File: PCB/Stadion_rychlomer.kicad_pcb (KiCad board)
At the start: 4 copper layers, 44 x 44 mm, 56 parts, among them J2 OLED I2C, J3 ICSP, J4 Conn_01x03_Pin, J5 SPÍD & PWR, J6 AUX DDAA, J7 ENG RPM, Q1 140817143200, Q2 PC817, U1 Mikroprofesor, U3 LM1117MP-5.0, Y1 16MHz

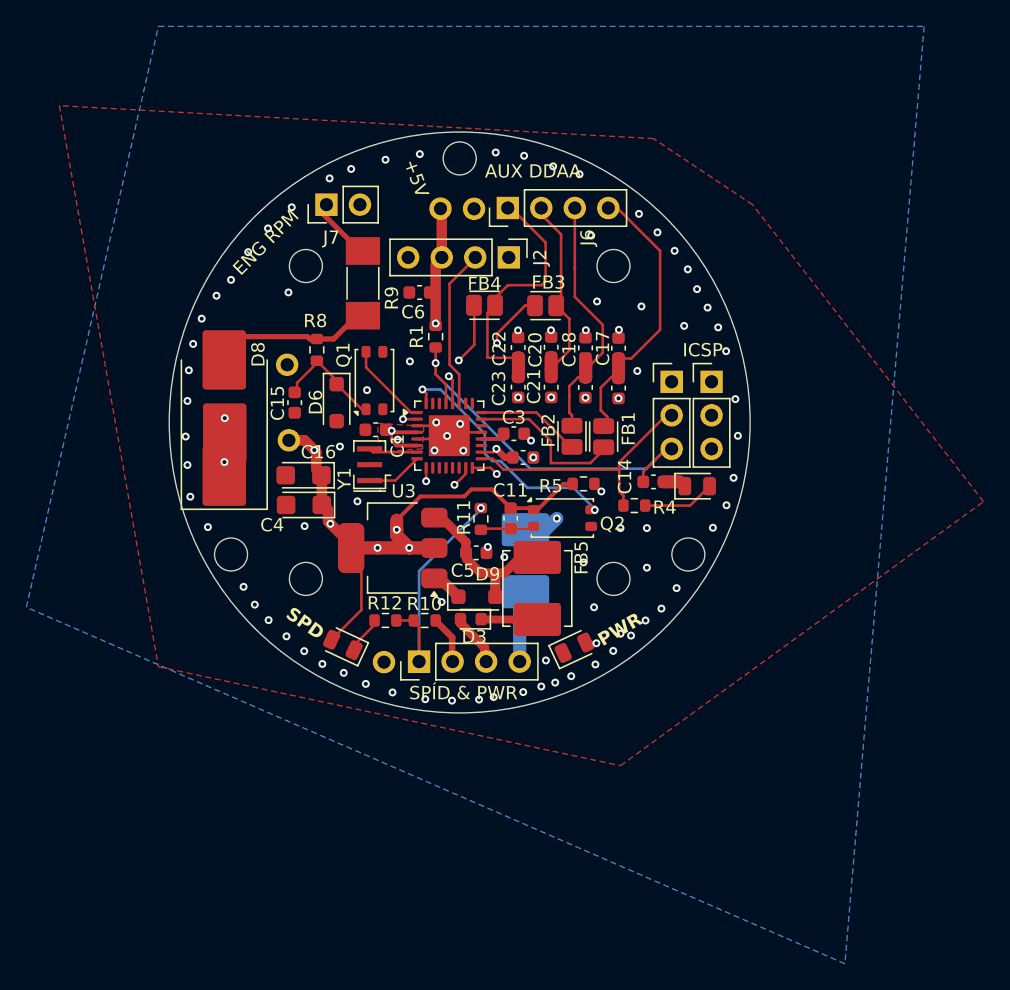
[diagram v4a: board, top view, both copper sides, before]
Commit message: SCL SDA Fixed, minor edits
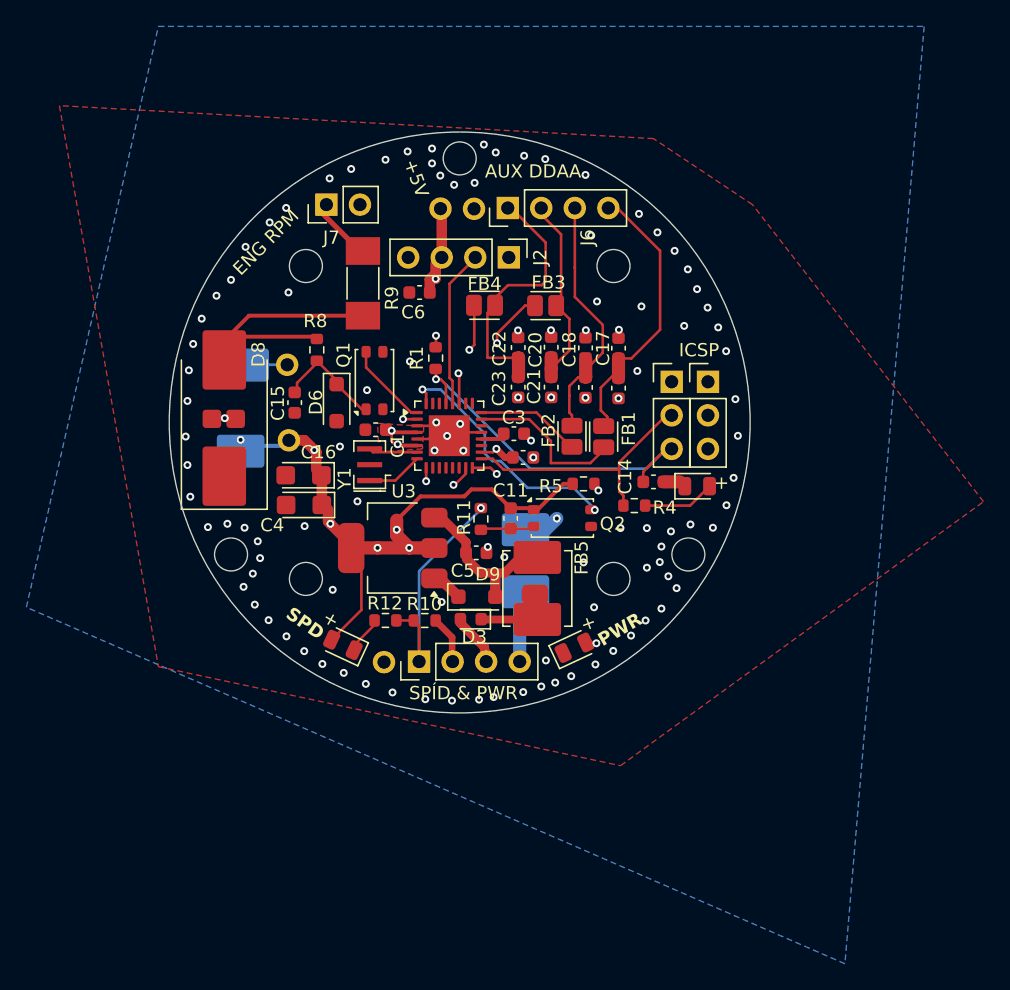
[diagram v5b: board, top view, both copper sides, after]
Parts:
- removed the ? at (100.0, 144.8)
- added ?: , , F.Cu at (123.5, 157.0)
- added ?: , , F.Cu at (101.2, 146.2)
- added ?: , , F.Cu at (100.8, 143.7)
- added ?: , , F.Cu at (99.0, 143.7)
- added ?: , , F.Cu at (101.6, 139.7)
- D9: value SMCJ85CA -> PTVS8V5S1UTR-QX
- FB5, FB6: value FerriteBead_Small -> FerriteBead_4A_180Ω
- moved R1 1.62 mm to (116.0, 139.1)
- moved J3 0.28 mm to (136.6, 140.9)
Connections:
- C5 pad 1: Net-(D9-A2) -> Net-(D9-K)
- D9 pad 1: GND -> Net-(D9-K)
- D9 pad 2: Net-(D9-A2) -> GND
- FB5 pad 2: Net-(D9-A2) -> Net-(D9-K)
- U1 pad 27: /I2C_SCL -> /I2C_SDA
- U1 pad 28: /I2C_SDA -> /I2C_SCL
- U3 pad 3: Net-(D9-A2) -> Net-(D9-K)
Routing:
- net +5V: track 118.4 -> 97.9 mm, vias 13 -> 15
- net GND: track 16.7 -> 32.1 mm, vias 92 -> 107
- net Net-(D9-A2): track 12.0 -> 0.00 mm
- net Net-(D8-A2): track 11.1 -> 20.1 mm
- net /I2C_SDA: track 16.7 -> 12.7 mm
- net /RESET_: track 29.8 -> 27.4 mm
- net /D4: track 14.9 -> 14.2 mm
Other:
- board text added: "+"
- board text added: "MOPeD JeSUS STADi-SPÍDo V2"
- board text removed: "MOPeD JeSUS STADi-SPÍDo V1"

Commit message: fix TVS na VIN
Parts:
- moved D9 0.06 mm to (119.1, 157.2), turned to 180 degrees
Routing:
- net Net-(D9-K): track 0.00 -> 12.0 mm
- net GND: track 32.1 -> 20.1 mm
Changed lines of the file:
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@@
 	(footprint "Diode_SMD:D_SOD-123F"
 		(layer "F.Cu")
-		(at 119.125 157.2)
+		(at 119.1 157.15 180)
 		(descr "D_SOD-123F")
 		(tags "D_SOD-123F")
 		(property "Reference" "D9"
-			(at 0.825 -1.7 0)
+			(at 0.825 -1.7 180)
 			(layer "F.SilkS")
 			(effects
@@
 		)
 		(property "Value" "PTVS8V5S1UTR-QX"
-			(at 0 2.1 0)
+			(at 0 2.1 180)
 			(layer "F.Fab")
 			(hide yes)
@@
 		)
 		(property "Datasheet" "https://assets.nexperia.com/documents/data-sheet/PTVSXS1UTR-Q_SER.pdf"
-			(at 0 0 0)
+			(at 0 0 180)
 			(unlocked yes)
 			(layer "F.Fab")
@@
 		)
 		(property "Description" "Ochranné diody proti elektrostatickým výbojům/diody pro potlačení napětí z přechodových jevů PTVS8V5S1UTR-Q/SOD123W/CFP3"
-			(at 0 0 0)
+			(at 0 0 180)
 			(unlocked yes)
 			(layer "F.Fab")
@@
 		)
 		(property "PN" " PTVS8V5S1UTR-QX "
-			(at 0 0 0)
+			(at 0 0 180)
 			(unlocked yes)
 			(layer "F.Fab")
@@
 		)
 		(property "Supplier PN" " 771-PTVS8V5S1UTR-QX "
-			(at 0 0 0)
+			(at 0 0 180)
 			(unlocked yes)
 			(layer "F.Fab")
@@
 		)
 		(property "Supplier" "Mouser Electronics"
-			(at 0 0 0)
+			(at 0 0 180)
 			(unlocked yes)
 			(layer "F.Fab")
@@
 		)
 		(property "JLCPCB Part" ""
-			(at 0 0 0)
+			(at 0 0 180)
 			(unlocked yes)
 			(layer "F.Fab")
@@
 		(duplicate_pad_numbers_are_jumpers no)
 		(fp_line
-			(start -2.21 -1)
-			(end -2.21 1)
+			(start -2.21 1)
+			(end 1.65 1)
 			(stroke
 				(width 0.12)
@@
 		)
 		(fp_line
-			(start -2.21 1)
-			(end 1.65 1)
+			(start -2.21 -1)
+			(end -2.21 1)
 			(stroke
 				(width 0.12)
@@
 		)
 		(fp_line
-			(start -2.2 -1.15)
+			(start 2.2 1.15)
 			(end -2.2 1.15)
 			(stroke
@@
 		)
 		(fp_line
-			(start -2.2 -1.15)
-			(end 2.2 -1.15)
+			(start 2.2 -1.15)
+			(end 2.2 1.15)
 			(stroke
 				(width 0.05)
@@
 		)
 		(fp_line
-			(start 2.2 -1.15)
-			(end 2.2 1.15)
+			(start -2.2 -1.15)
+			(end 2.2 -1.15)
 			(stroke
 				(width 0.05)
@@
 		)
 		(fp_line
-			(start 2.2 1.15)
+			(start -2.2 -1.15)
 			(end -2.2 1.15)
 			(stroke
@@
 		)
 		(fp_line
-			(start -1.4 -0.9)
-			(end 1.4 -0.9)
+			(start 1.4 0.9)
+			(end -1.4 0.9)
 			(stroke
 				(width 0.1)
@@
 		)
 		(fp_line
-			(start -1.4 0.9)
-			(end -1.4 -0.9)
+			(start 1.4 -0.9)
+			(end 1.4 0.9)
 			(stroke
 				(width 0.1)
@@
 		)
 		(fp_line
-			(start -0.75 0)
+			(start 0.25 0.4)
 			(end -0.35 0)
 			(stroke
@@
 		)
 		(fp_line
-			(start -0.35 0)
-			(end -0.35 -0.55)
+			(start 0.25 0)
+			(end 0.75 0)
 			(stroke
 				(width 0.1)
@@
 		)
 		(fp_line
-			(start -0.35 0)
-			(end -0.35 0.55)
+			(start 0.25 -0.4)
+			(end 0.25 0.4)
 			(stroke
 				(width 0.1)
@@
 		)
 		(fp_line
-			(start 0.25 -0.4)
-			(end 0.25 0.4)
+			(start -0.35 0)
+			(end -0.35 0.55)
 			(stroke
 				(width 0.1)
@@
 		)
 		(fp_line
-			(start 0.25 0)
-			(end 0.75 0)
+			(start -0.35 0)
+			(end -0.35 -0.55)
 			(stroke
 				(width 0.1)
@@
 		)
 		(fp_line
-			(start 0.25 0.4)
+			(start -0.75 0)
 			(end -0.35 0)
 			(stroke
@@
 		)
 		(fp_line
-			(start 1.4 -0.9)
-			(end 1.4 0.9)
+			(start -1.4 0.9)
+			(end -1.4 -0.9)
 			(stroke
 				(width 0.1)
@@
 		)
 		(fp_line
-			(start 1.4 0.9)
-			(end -1.4 0.9)
+			(start -1.4 -0.9)
+			(end 1.4 -0.9)
 			(stroke
 				(width 0.1)
@@
 		)
 		(fp_text user "${REFERENCE}"
-			(at 0.825 -1.7 0)
+			(at 0.825 -1.7 180)
 			(layer "F.Fab")
 			(effects
@@
 		)
 		(pad "1" smd roundrect
-			(at -1.4 0)
+			(at -1.4 0 180)
 			(size 1.1 1.1)
 			(layers "F.Cu" "F.Mask" "F.Paste")
@@
 		)
 		(pad "2" smd roundrect
-			(at 1.4 0)
+			(at 1.4 0 180)
 			(size 1.1 1.1)
 			(layers "F.Cu" "F.Mask" "F.Paste")
@@
 	)
 	(segment
-		(start 116.15 151.2)
-		(end 116.425 151.2)
-		(width 0.5)
-		(layer "F.Cu")
-		(net "GND")
-	)
-	(segment
 		(start 117 144.97)
 		(end 116.28 144.25)
@@
 	)
 	(segment
-		(start 120.525 157.2)
-		(end 120.525 155.475)
-		(width 0.8)
-		(layer "F.Cu")
-		(net "GND")
-	)
-	(segment
 		(start 113.46 131.96)
 		(end 113.92 131.5)
@@
 	)
 	(segment
-		(start 120.6 155.4)
-		(end 121.225 155.4)
-		(width 0.7)
-		(layer "F.Cu")
-		(net "GND")
-	)
-	(segment
 		(start 116.953114 145.076886)
 		(end 116.78 145.25)
@@
 	)
 	(segment
-		(start 121.225 155.4)
-		(end 122.325 154.3)
-		(width 0.7)
-		(layer "F.Cu")
-		(net "GND")
-	)
-	(segment
 		(start 116.840735 145.189265)
 		(end 115.531765 145.189265)
@@
 	)
 	(segment
-		(start 122.325 154.3)
-		(end 123.4 154.3)
-		(width 0.7)
-		(layer "F.Cu")
-		(net "GND")
-	)
-	(segment
 		(start 117 145.016943)
 		(end 117 144.97)
@@
 	)
 	(segment
-		(start 120.525 155.475)
-		(end 120.6 155.4)
-		(width 0.2)
-		(layer "F.Cu")
-		(net "GND")
-	)
-	(segment
 		(start 117.725 157.2)
 		(end 116.3375 155.8125)
@@
 	)
 	(segment
-		(start 118.3 153.075)
-		(end 118.3 153.875)
-		(width 0.7)
-		(layer "F.Cu")
-		(net "GND")
-	)
-	(segment
 		(start 114.225 131.195)
 		(end 113.92 131.5)
@@
 	)
 	(segment
-		(start 119.4 155.4)
-		(end 120.6 155.4)
-		(width 0.7)
-		(layer "F.Cu")
-		(net "GND")
-	)
-	(segment
-		(start 118.35 153.925)
-		(end 118.35 154.35)
-		(width 0.7)
-		(layer "F.Cu")
-		(net "GND")
-	)
-	(segment
 		(start 112.131372 143)
 		(end 112 143)
@@
 	)
 	(segment
-		(start 118.3 153.875)
-		(end 118.35 153.925)
-		(width 0.7)
-		(layer "F.Cu")
-		(net "GND")
-	)
-	(segment
 		(start 117 145.03)
 		(end 116.953114 145.076886)
@@
 		(net "GND")
 	)
-	(segment
-		(start 118.35 154.35)
-		(end 119.4 155.4)
-		(width 0.7)
-		(layer "F.Cu")
-		(net "GND")
-	)
-	(segment
-		(start 116.425 151.2)
-		(end 118.3 153.075)
-		(width 0.7)
-		(layer "F.Cu")
-		(net "GND")
-	)
 	(via
 		(at 131.4 128.2)
@@
 	)
 	(segment
+		(start 116.15 151.2)
+		(end 116.425 151.2)
+		(width 0.5)
+		(layer "F.Cu")
+		(net "Net-(D9-K)")
+	)
+	(segment
+		(start 120.525 157.2)
+		(end 120.525 155.475)
+		(width 0.8)
+		(layer "F.Cu")
+		(net "Net-(D9-K)")
+	)
+	(segment
+		(start 120.6 155.4)
+		(end 121.225 155.4)
+		(width 0.7)
+		(layer "F.Cu")
+		(net "Net-(D9-K)")
+	)
+	(segment
+		(start 121.225 155.4)
+		(end 122.325 154.3)
+		(width 0.7)
+		(layer "F.Cu")
+		(net "Net-(D9-K)")
+	)
+	(segment
+		(start 122.325 154.3)
+		(end 123.4 154.3)
+		(width 0.7)
+		(layer "F.Cu")
+		(net "Net-(D9-K)")
+	)
+	(segment
+		(start 120.525 155.475)
+		(end 120.6 155.4)
+		(width 0.2)
+		(layer "F.Cu")
+		(net "Net-(D9-K)")
+	)
+	(segment
+		(start 118.3 153.075)
+		(end 118.3 153.875)
+		(width 0.7)
+		(layer "F.Cu")
+		(net "Net-(D9-K)")
+	)
+	(segment
+		(start 119.4 155.4)
+		(end 120.6 155.4)
+		(width 0.7)
+		(layer "F.Cu")
+		(net "Net-(D9-K)")
+	)
+	(segment
+		(start 118.35 153.925)
+		(end 118.35 154.35)
+		(width 0.7)
+		(layer "F.Cu")
+		(net "Net-(D9-K)")
+	)
+	(segment
+		(start 118.3 153.875)
+		(end 118.35 153.925)
+		(width 0.7)
+		(layer "F.Cu")
+		(net "Net-(D9-K)")
+	)
+	(segment
+		(start 118.35 154.35)
+		(end 119.4 155.4)
+		(width 0.7)
+		(layer "F.Cu")
+		(net "Net-(D9-K)")
+	)
+	(segment
+		(start 116.425 151.2)
+		(end 118.3 153.075)
+		(width 0.7)
+		(layer "F.Cu")
+		(net "Net-(D9-K)")
+	)
+	(segment
